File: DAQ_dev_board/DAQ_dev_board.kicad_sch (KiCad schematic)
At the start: 30 parts, among them J1 Thermocouple, J2 A0, A1, J3 GPIO1, J4 DOUT, DRDY, J5 SCLK, DIN, J6 START, CS, J7 RESET, PDWN, U1 ADS1158IRTCR (ADC), U2 AD8495 (TC AMP), U3 OP777ARZ (OP AMP), Y1 32.768kHz

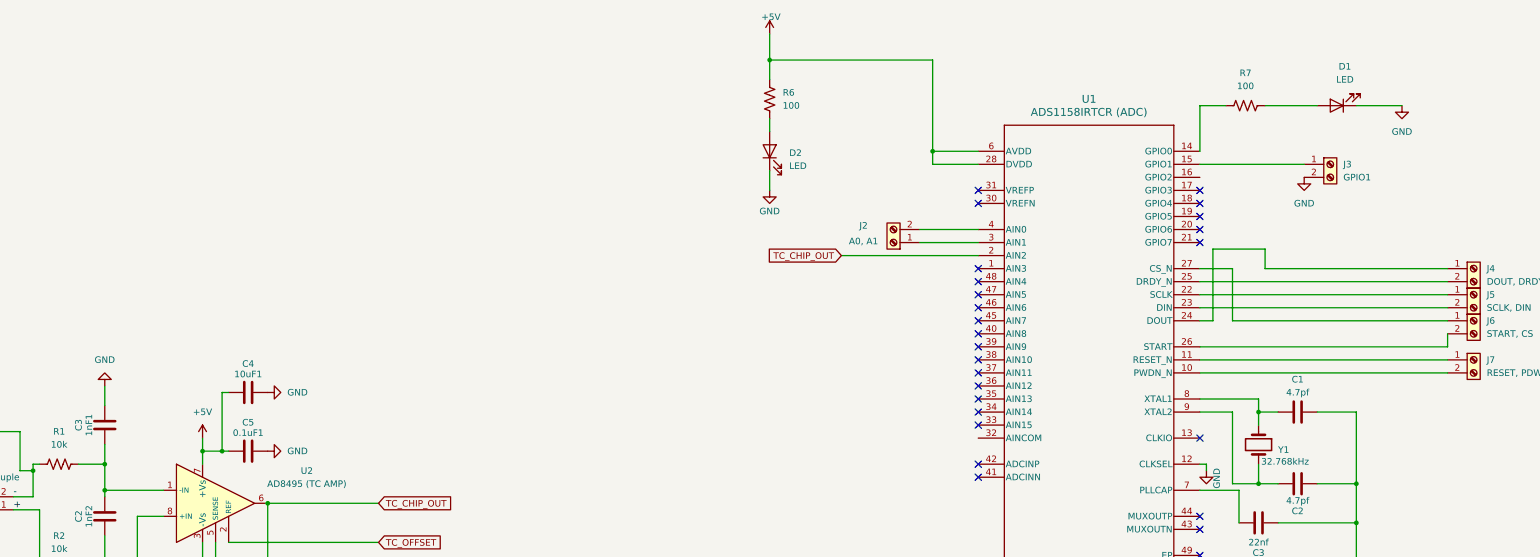
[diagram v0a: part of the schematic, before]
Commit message: updated pinout and other fixes
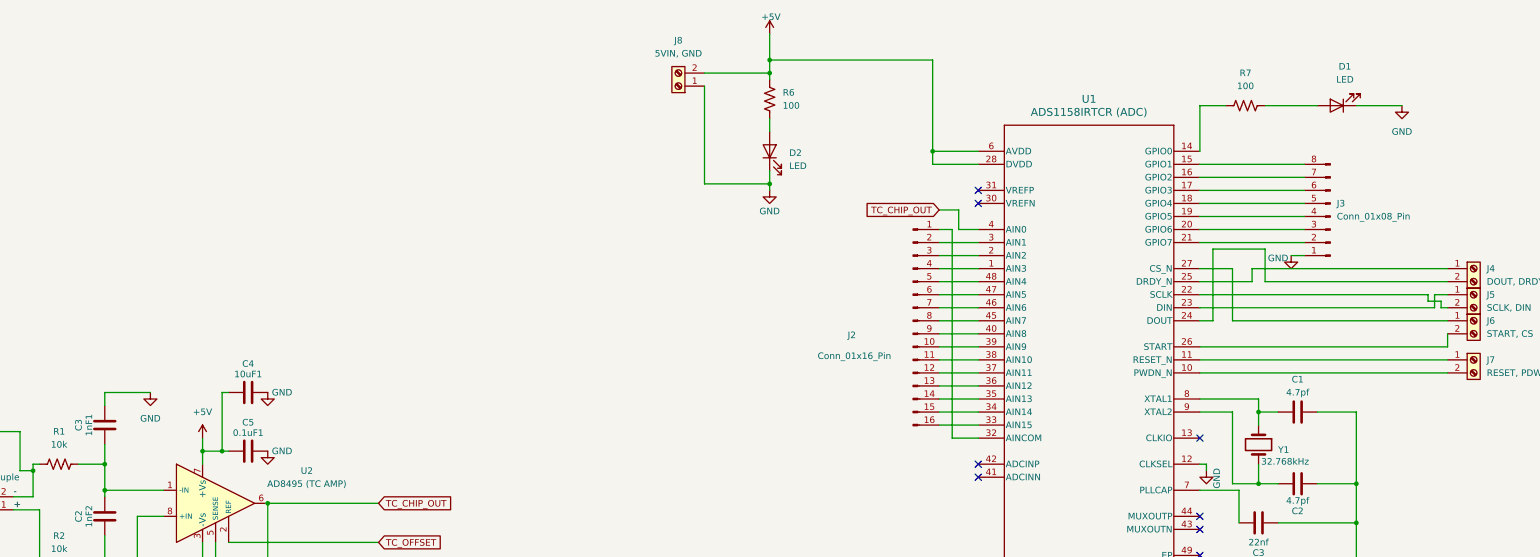
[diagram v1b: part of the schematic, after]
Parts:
- removed J2: A0, A1, TerminalBlock:TerminalBlock_Xinya_XY308-2.54-2P_1x02_P2.54mm_Horizontal, symbol Connector:Screw_Terminal_01x02
- removed J3: GPIO1, TerminalBlock:TerminalBlock_Xinya_XY308-2.54-2P_1x02_P2.54mm_Horizontal, symbol Connector:Screw_Terminal_01x02
- added J2: Conn_01x16_Pin, Connector_PinHeader_2.54mm:PinHeader_1x16_P2.54mm_Vertical, symbol Connector:Conn_01x16_Pin
- added J3: Conn_01x08_Pin, Connector_PinHeader_2.54mm:PinHeader_1x08_P2.54mm_Vertical, symbol Connector:Conn_01x08_Pin
- added J8: 5VIN, GND, TerminalBlock:TerminalBlock_Xinya_XY308-2.54-2P_1x02_P2.54mm_Horizontal, symbol Connector:Screw_Terminal_01x02
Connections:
- net +5V: now also J8.2 (Pin_2)
- net GND: now also J3.1 (Pin_1), J8.1 (Pin_1)
- net TC_CHIP_OUT: now also U1.4 (AIN0); no longer U1.2 (AIN2)
- net at U1.3 (AIN1): now also J2.2 (Pin_2)
- net at U1.1 (AIN3): now also J2.4 (Pin_4)
- net at U1.15 (GPIO1): now also J3.8 (Pin_8)
- net at U1.16 (GPIO2): now also J3.7 (Pin_7)
- net at U1.17 (GPIO3): now also J3.6 (Pin_6)
- net at U1.18 (GPIO4): now also J3.5 (Pin_5)
- net at U1.19 (GPIO5): now also J3.4 (Pin_4)
- net at U1.20 (GPIO6): now also J3.3 (Pin_3)
- net at U1.21 (GPIO7): now also J3.2 (Pin_2)
- net at U1.22 (SCLK): now also J5.2 (Pin_2); no longer J5.1 (Pin_1)
- net at U1.23 (DIN): now also J5.1 (Pin_1); no longer J5.2 (Pin_2)
- net at U1.24 (DOUT): now also J4.2 (Pin_2); no longer J4.1 (Pin_1)
- net at U1.25 (DRDY_N): now also J4.1 (Pin_1); no longer J4.2 (Pin_2)
- net at U1.32 (AINCOM): now also J2.1 (Pin_1)
- net at U1.33 (AIN15): now also J2.16 (Pin_16)
- net at U1.34 (AIN14): now also J2.15 (Pin_15)
- net at U1.35 (AIN13): now also J2.14 (Pin_14)
- net at U1.36 (AIN12): now also J2.13 (Pin_13)
- net at U1.37 (AIN11): now also J2.12 (Pin_12)
- net at U1.38 (AIN10): now also J2.11 (Pin_11)
- net at U1.39 (AIN9): now also J2.10 (Pin_10)
- net at U1.40 (AIN8): now also J2.9 (Pin_9)
- net at U1.45 (AIN7): now also J2.8 (Pin_8)
- net at U1.46 (AIN6): now also J2.7 (Pin_7)
- net at U1.47 (AIN5): now also J2.6 (Pin_6)
- net at U1.48 (AIN4): now also J2.5 (Pin_5)
- new net: J2.3 (Pin_3), U1.2 (AIN2)
- no-connect marks 26 -> 8

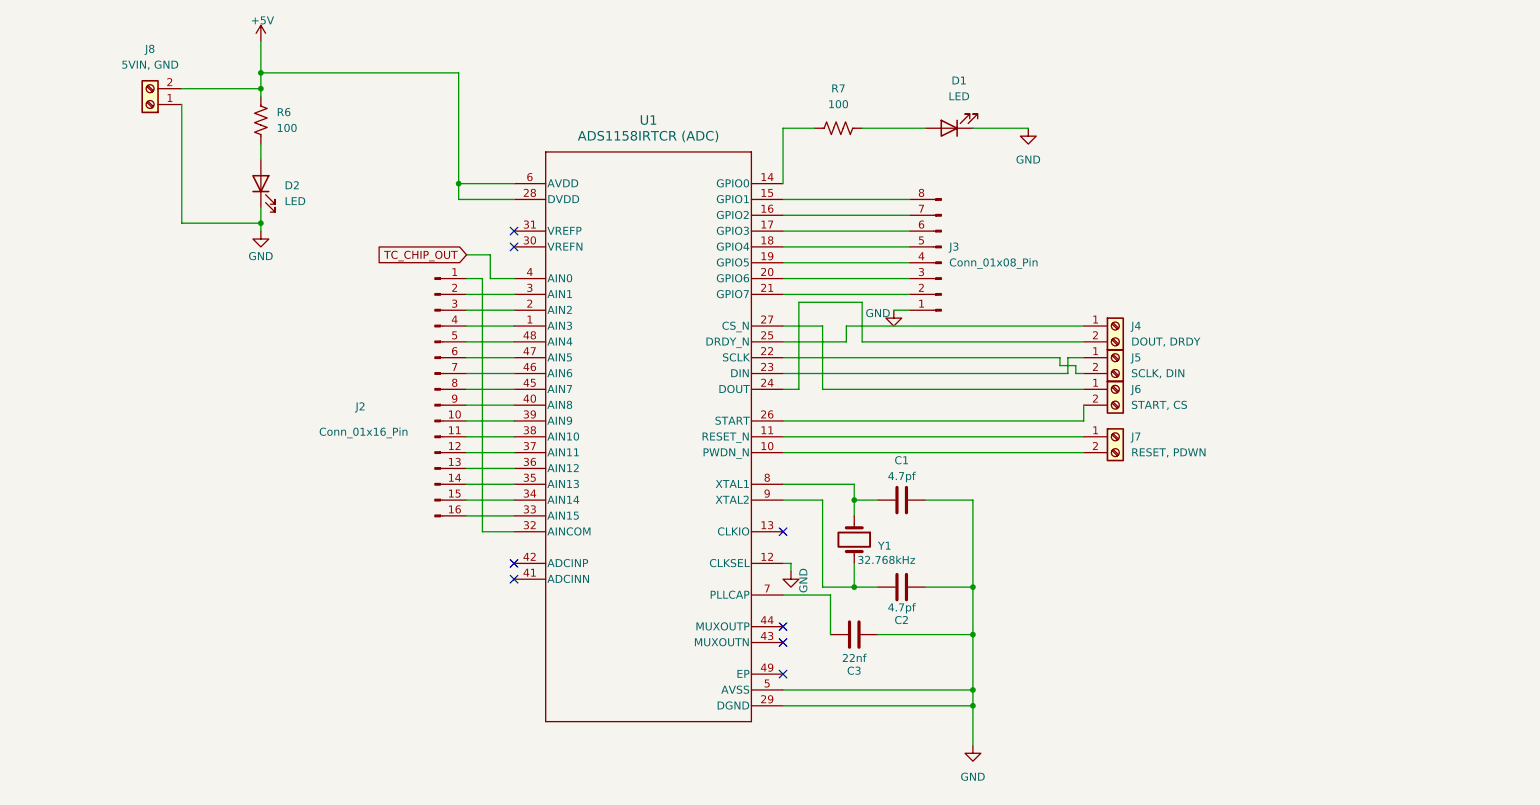
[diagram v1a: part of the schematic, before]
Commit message: added pulldowns and replaced screw terminals with header pins
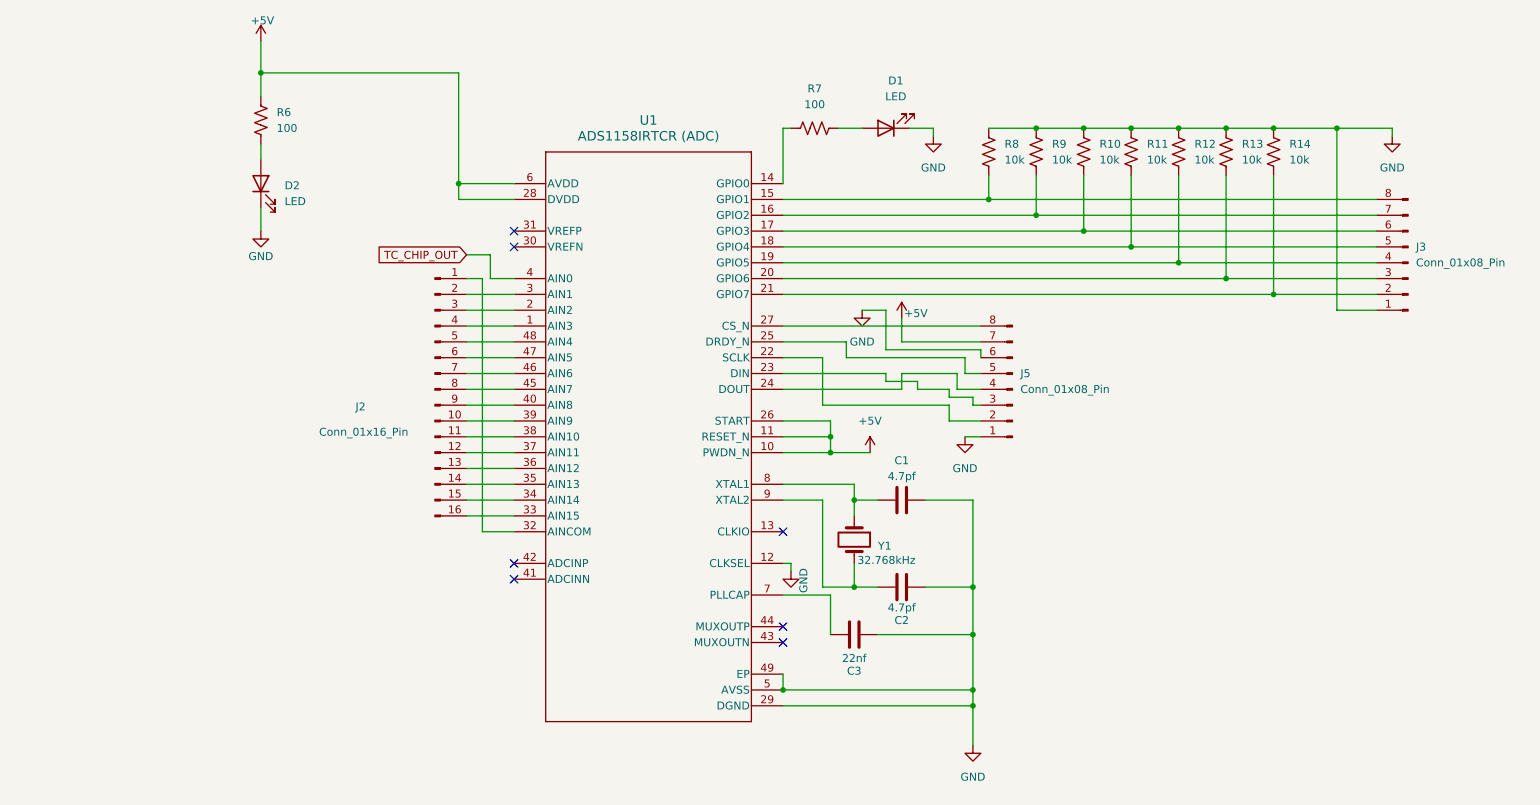
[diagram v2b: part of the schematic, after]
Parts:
- removed J4: DOUT, DRDY, TerminalBlock:TerminalBlock_Xinya_XY308-2.54-2P_1x02_P2.54mm_Horizontal, symbol Connector:Screw_Terminal_01x02
- removed J5: SCLK, DIN, TerminalBlock:TerminalBlock_Xinya_XY308-2.54-2P_1x02_P2.54mm_Horizontal, symbol Connector:Screw_Terminal_01x02
- removed J6: START, CS, TerminalBlock:TerminalBlock_Xinya_XY308-2.54-2P_1x02_P2.54mm_Horizontal, symbol Connector:Screw_Terminal_01x02
- removed J7: RESET, PDWN, TerminalBlock:TerminalBlock_Xinya_XY308-2.54-2P_1x02_P2.54mm_Horizontal, symbol Connector:Screw_Terminal_01x02
- removed J8: 5VIN, GND, TerminalBlock:TerminalBlock_Xinya_XY308-2.54-2P_1x02_P2.54mm_Horizontal, symbol Connector:Screw_Terminal_01x02
- added J5: Conn_01x08_Pin, Connector_PinHeader_2.54mm:PinHeader_1x08_P2.54mm_Vertical, symbol Connector:Conn_01x08_Pin
- added R10, R11, R12, R13, R14, R8, R9: 10k, Capacitor_SMD:C_0603_1608Metric, symbol Device:R_US
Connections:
- net +5V: now also U1.10 (PWDN_N), U1.11 (RESET_N), U1.26 (START), J5.7 (Pin_7)
- net GND: now also U1.49 (EP), J5.1 (Pin_1), J5.6 (Pin_6), R10.1, R11.1, R12.1, R13.1, R14.1, R8.1, R9.1
- net at J3.8 (Pin_8), U1.15 (GPIO1): now also R8.2
- net at J3.7 (Pin_7), U1.16 (GPIO2): now also R9.2
- net at J3.6 (Pin_6), U1.17 (GPIO3): now also R10.2
- net at J3.5 (Pin_5), U1.18 (GPIO4): now also R11.2
- net at J3.4 (Pin_4), U1.19 (GPIO5): now also R12.2
- net at J3.3 (Pin_3), U1.20 (GPIO6): now also R13.2
- net at J3.2 (Pin_2), U1.21 (GPIO7): now also R14.2
- net at U1.22 (SCLK): now also J5.2 (Pin_2)
- net at U1.23 (DIN): now also J5.3 (Pin_3)
- net at U1.24 (DOUT): now also J5.4 (Pin_4)
- net at U1.25 (DRDY_N): now also J5.5 (Pin_5)
- net at U1.27 (CS_N): now also J5.8 (Pin_8)
- no-connect marks 8 -> 7
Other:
- moved on the sheet: D1, J3, R7

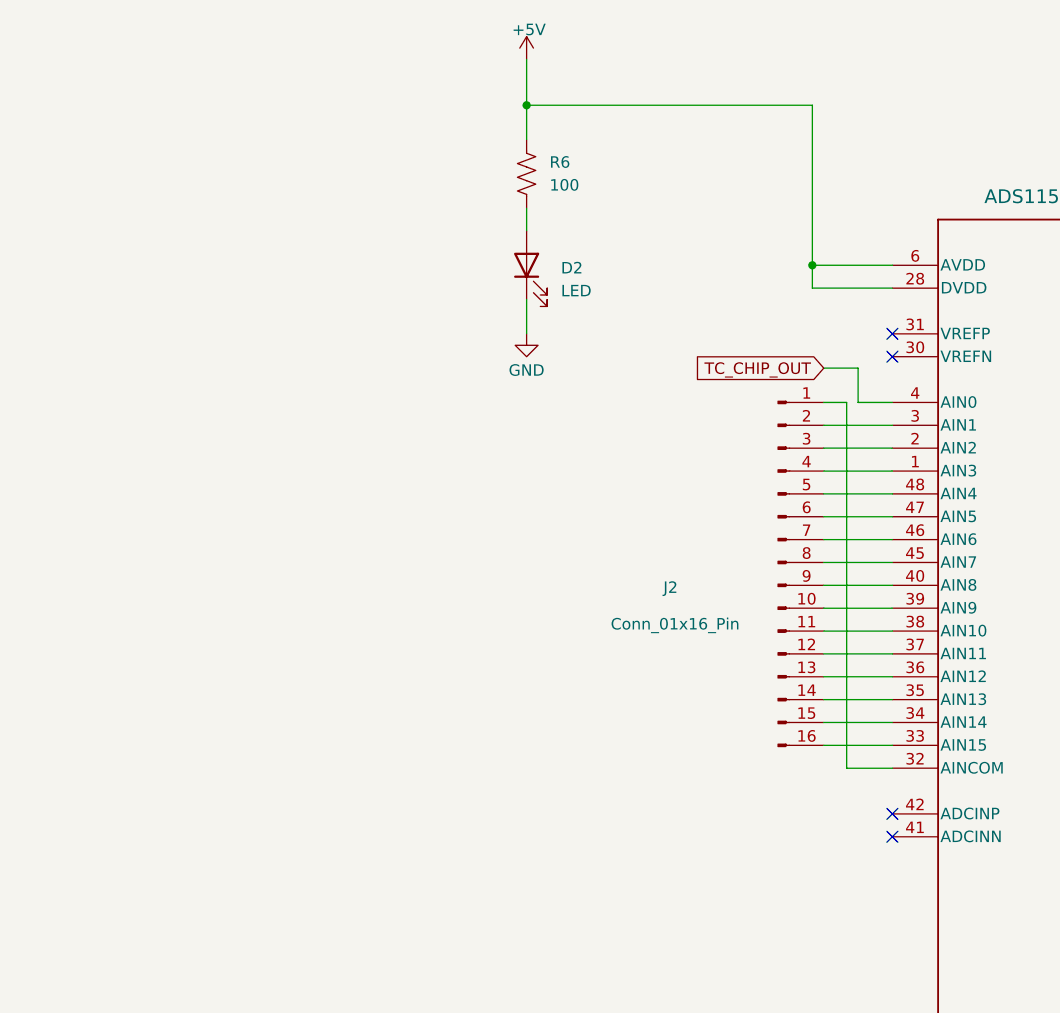
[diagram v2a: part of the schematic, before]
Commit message: Minor Fixes
List of changes
Grounded AINCOM
Added 0.1uF and 10uF decoupling between AVDD/DVDD to ground.
Added capacitor for reference inputs (pg. 39) , also not sure how we missed this earlier but VREFP and VREFN have to have reference inputs so I fixed that
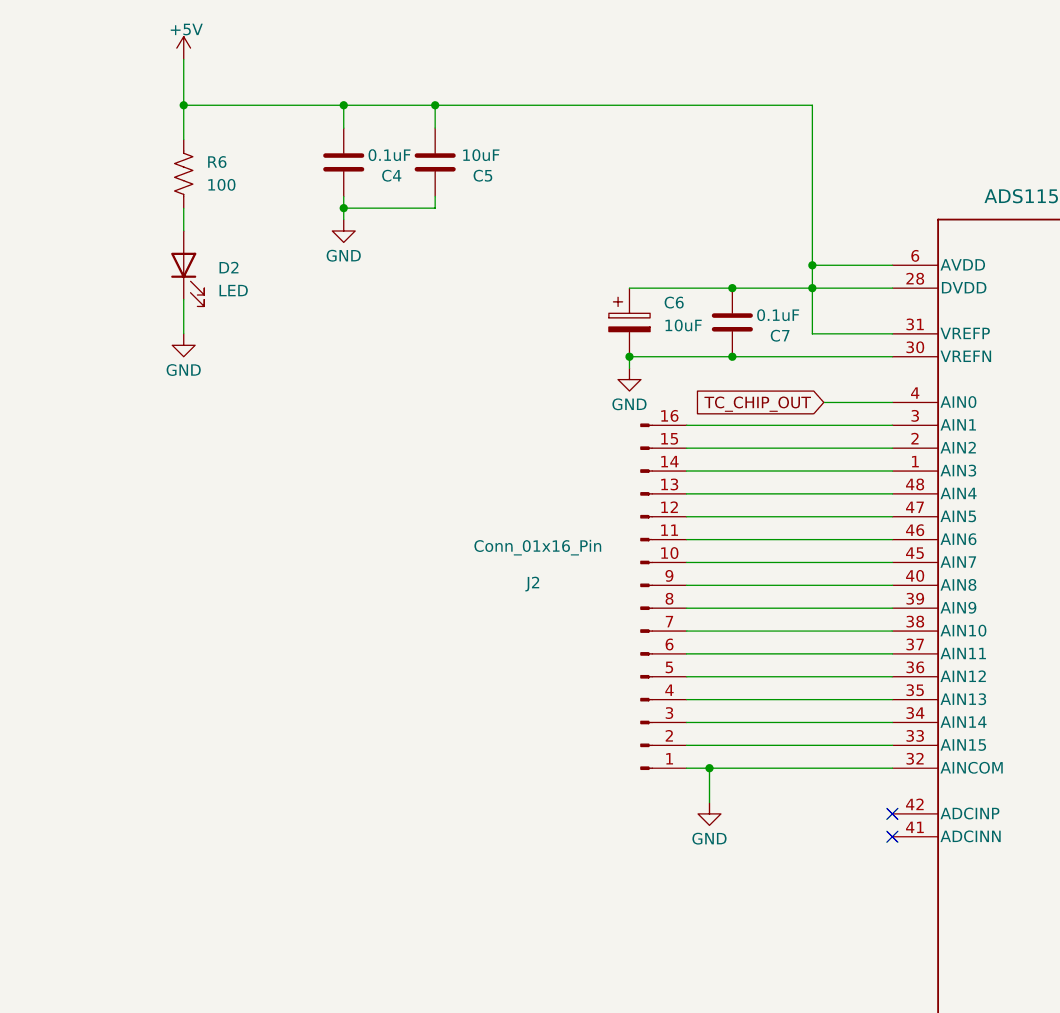
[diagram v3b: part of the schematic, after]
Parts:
- added C4, C7: 0.1uF, Capacitor_SMD:C_0603_1608Metric, symbol Device:C
- added C5: 10uF, Capacitor_SMD:C_0603_1608Metric, symbol Device:C
- added C6: 10uF, symbol Device:C_Polarized
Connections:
- net +5V: now also U1.31 (VREFP), C4.1, C5.1, C6.1, C7.1
- net GND: now also J2.1 (Pin_1), U1.30 (VREFN), U1.32 (AINCOM), C4.2, C5.2, C6.2, C7.2
- net at U1.1 (AIN3): now also J2.14 (Pin_14); no longer J2.4 (Pin_4)
- net at U1.2 (AIN2): now also J2.15 (Pin_15); no longer J2.3 (Pin_3)
- net at U1.3 (AIN1): now also J2.16 (Pin_16); no longer J2.2 (Pin_2)
- net at U1.33 (AIN15): now also J2.2 (Pin_2); no longer J2.16 (Pin_16)
- net at U1.34 (AIN14): now also J2.3 (Pin_3); no longer J2.15 (Pin_15)
- net at U1.35 (AIN13): now also J2.4 (Pin_4); no longer J2.14 (Pin_14)
- net at U1.36 (AIN12): now also J2.5 (Pin_5); no longer J2.13 (Pin_13)
- net at U1.37 (AIN11): now also J2.6 (Pin_6); no longer J2.12 (Pin_12)
- net at U1.38 (AIN10): now also J2.7 (Pin_7); no longer J2.11 (Pin_11)
- net at U1.39 (AIN9): now also J2.8 (Pin_8); no longer J2.10 (Pin_10)
- net at U1.45 (AIN7): now also J2.10 (Pin_10); no longer J2.8 (Pin_8)
- net at U1.46 (AIN6): now also J2.11 (Pin_11); no longer J2.7 (Pin_7)
- net at U1.47 (AIN5): now also J2.12 (Pin_12); no longer J2.6 (Pin_6)
- net at U1.48 (AIN4): now also J2.13 (Pin_13); no longer J2.5 (Pin_5)
- no-connect marks 7 -> 5
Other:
- moved on the sheet: D2, J2, R6
